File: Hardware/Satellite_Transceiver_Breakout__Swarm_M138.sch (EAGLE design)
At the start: 61 parts, among them Q2 20V/4.2A/52mΩ/1.4W, Q4 20V/4.2A/52mΩ/1.4W, U1 CH340E_MSOP10, U2 SWARM_M138_TRANSCEIVER_MAIN, U3 STLQ015-3.3V

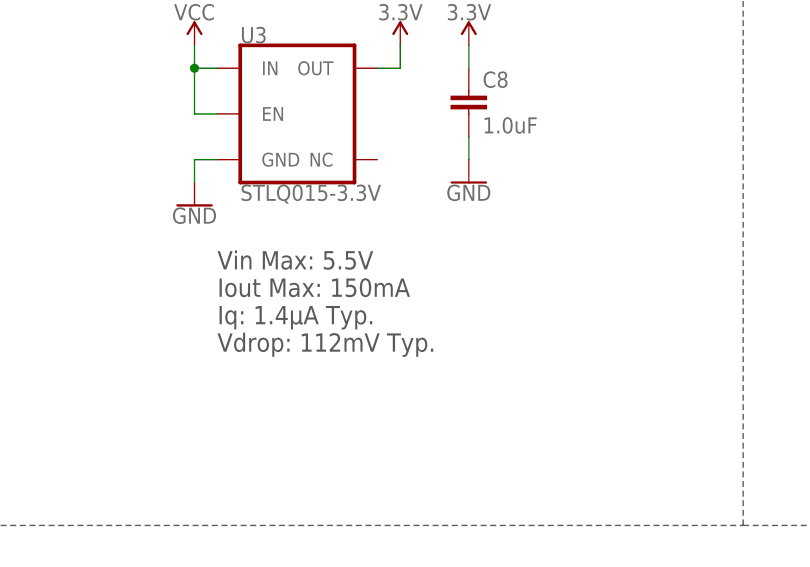
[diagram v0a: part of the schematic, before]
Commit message: Replace 3.3V Reg with AP2112K
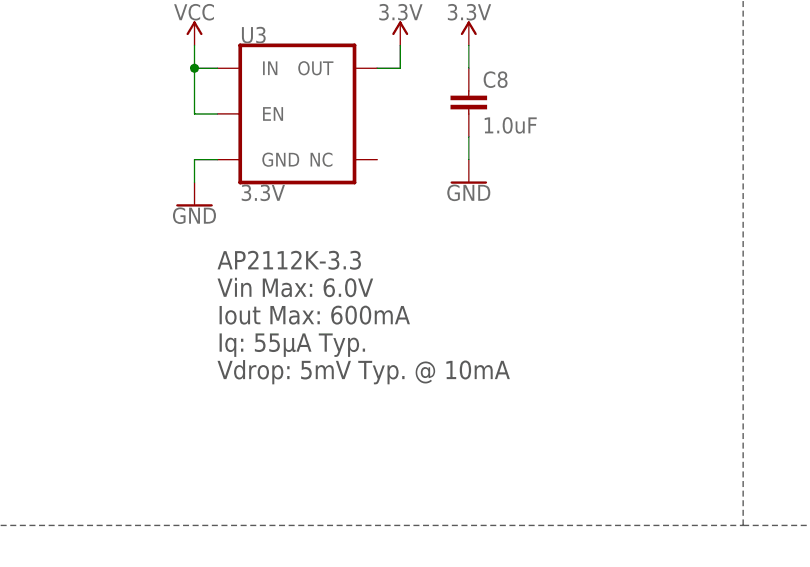
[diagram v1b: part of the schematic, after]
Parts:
- U3: value STLQ015-3.3V -> 3.3V; device SparkFun-IC-Power:STLQ015-3.3V -> SparkFun-IC-Power:V_REG_AP2112K-3.3V
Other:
- note added: "AP2112K-3.3 Vin Max: 6.0V Iout Max: 600mA Iq: 55µA Typ. Vdrop: 5mV Typ. @ 10mA"
- note removed: "Vin Max: 5.5V Iout Max: 150mA Iq: 1.4µA Typ. Vdrop: 112mV Typ."
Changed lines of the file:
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@@
 <part name="C5" library="SparkFun-Capacitors" deviceset="100UF-POLAR" device="-25V-20%(ELEC)" value="100uF"/>
 <part name="U2" library="Swarm" deviceset="SWARM_M138_TRANSCEIVER" device="_MAIN"/>
-<part name="U3" library="SparkFun-IC-Power" deviceset="STLQ015" device="-3.3V"/>
+<part name="U3" library="SparkFun-IC-Power" deviceset="V_REG_AP2112" device="K-3.3V" value="3.3V"/>
 <part name="SUPPLY14" library="SparkFun-PowerSymbols" deviceset="VCC" device=""/>
 <part name="GND12" library="SparkFun-PowerSymbols" deviceset="GND" device=""/>
@@
 <text x="365.76" y="129.54" size="2.032" layer="97" font="vector" align="top-left">USB 2.0 is not supported
 Peak USB current draw is 600mA</text>
-<text x="160.02" y="144.78" size="2.032" layer="97" font="vector" align="top-left">Vin Max: 5.5V
-Iout Max: 150mA
-Iq: 1.4µA Typ.
-Vdrop: 112mV Typ.</text>
+<text x="160.02" y="144.78" size="2.032" layer="97" font="vector" align="top-left">AP2112K-3.3
+Vin Max: 6.0V
+Iout Max: 600mA
+Iq: 55µA Typ.
+Vdrop: 5mV Typ. @ 10mA</text>
 </plain>
 <instances>
@@
 <attribute name="VALUE" x="342.9" y="215.9" size="1.778" layer="96"/>
 </instance>
-<instance part="U3" gate="U1" x="170.18" y="160.02" smashed="yes">
+<instance part="U3" gate="G$1" x="170.18" y="160.02" smashed="yes">
 <attribute name="NAME" x="162.56" y="167.894" size="1.778" layer="95" font="vector"/>
 <attribute name="VALUE" x="162.56" y="152.146" size="1.778" layer="96" font="vector" align="top-left"/>
@@
 </segment>
 <segment>
-<pinref part="U3" gate="U1" pin="GND"/>
+<pinref part="U3" gate="G$1" pin="GND"/>
 <wire x1="160.02" y1="154.94" x2="157.48" y2="154.94" width="0.1524" layer="91"/>
 <pinref part="GND12" gate="1" pin="GND"/>
@@
 </segment>
 <segment>
-<pinref part="U3" gate="U1" pin="IN"/>
+<pinref part="U3" gate="G$1" pin="IN"/>
 <wire x1="160.02" y1="165.1" x2="157.48" y2="165.1" width="0.1524" layer="91"/>
 <pinref part="SUPPLY14" gate="G$1" pin="VCC"/>
 <wire x1="157.48" y1="165.1" x2="157.48" y2="167.64" width="0.1524" layer="91"/>
-<pinref part="U3" gate="U1" pin="EN"/>
+<pinref part="U3" gate="G$1" pin="EN"/>
 <wire x1="160.02" y1="160.02" x2="157.48" y2="160.02" width="0.1524" layer="91"/>
 <wire x1="157.48" y1="160.02" x2="157.48" y2="165.1" width="0.1524" layer="91"/>
@@
 <net name="3.3V" class="0">
 <segment>
-<pinref part="U3" gate="U1" pin="OUT"/>
+<pinref part="U3" gate="G$1" pin="OUT"/>
 <wire x1="177.8" y1="165.1" x2="180.34" y2="165.1" width="0.1524" layer="91"/>
 <pinref part="SUPPLY17" gate="G$1" pin="3.3V"/>

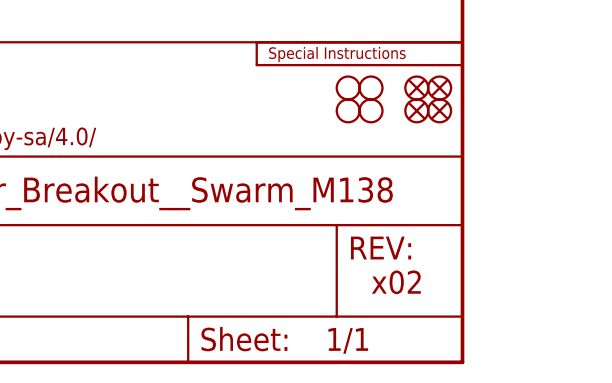
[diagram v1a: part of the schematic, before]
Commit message: Updates for x03 PCB - move standoffs by 0.6mm and add route-out gaps in panel
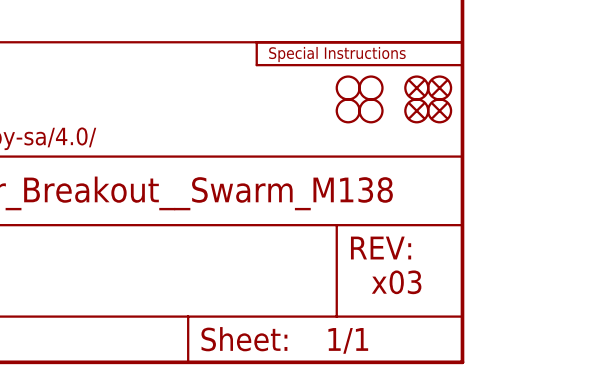
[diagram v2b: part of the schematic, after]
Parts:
- U2: device Swarm:SWARM_M138_TRANSCEIVER_MAIN -> SparkFun-RF:SWARM_M138_TRANSCEIVER_MAIN
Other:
- note added: "x03"
- note removed: "x02"
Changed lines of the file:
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@@
 <setting verticaltext="up"/>
 </settings>
-<grid distance="0.1" unitdist="inch" unit="inch" style="lines" multiple="1" display="no" altdistance="0.05" altunitdist="inch" altunit="inch"/>
+<grid distance="2.5" unitdist="mm" unit="mm" style="lines" multiple="1" display="no" altdistance="0.5" altunitdist="mm" altunit="mm"/>
 <layers>
 <layer number="1" name="Top" color="4" fill="1" visible="no" active="no"/>
@@
 <part name="C4" library="SparkFun-Capacitors" deviceset="100UF-POLAR" device="-25V-20%(ELEC)" value="100uF"/>
 <part name="C5" library="SparkFun-Capacitors" deviceset="100UF-POLAR" device="-25V-20%(ELEC)" value="100uF"/>
-<part name="U2" library="Swarm" deviceset="SWARM_M138_TRANSCEIVER" device="_MAIN"/>
+<part name="U2" library="SparkFun-RF" deviceset="SWARM_M138_TRANSCEIVER" device="_MAIN"/>
 <part name="U3" library="SparkFun-IC-Power" deviceset="V_REG_AP2112" device="K-3.3V" value="3.3V"/>
 <part name="SUPPLY14" library="SparkFun-PowerSymbols" deviceset="VCC" device=""/>
@@
 <sheet>
 <plain>
-<text x="421.64" y="7.62" size="2.54" layer="94" font="vector">x02</text>
+<text x="421.64" y="7.62" size="2.54" layer="94" font="vector">x03</text>
 <text x="350.52" y="10.16" size="2.54" layer="94" font="vector">Paul Clark</text>
 <text x="5.08" y="271.78" size="2.54" layer="94" font="vector">USB</text>
